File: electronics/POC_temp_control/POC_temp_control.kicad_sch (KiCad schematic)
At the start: 210 parts, among them J1 Conn_01x02, J2 Conn_01x07, J3 Conn_01x05, J4 Conn_01x06, J5 Conn_01x04, J6 Conn_01x06, Q1 PXT8050, Q10 BC847A, Q11 BC858B, Q12 BC847A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

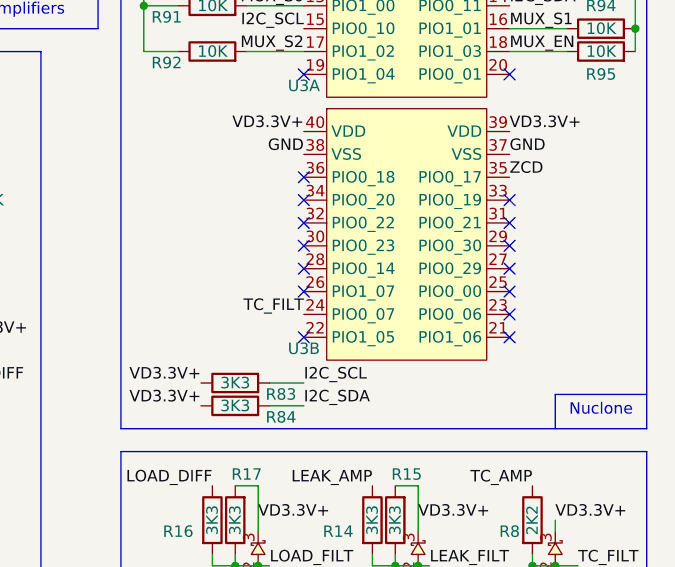
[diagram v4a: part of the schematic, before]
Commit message: further work on place and route, fixed some things with schematic
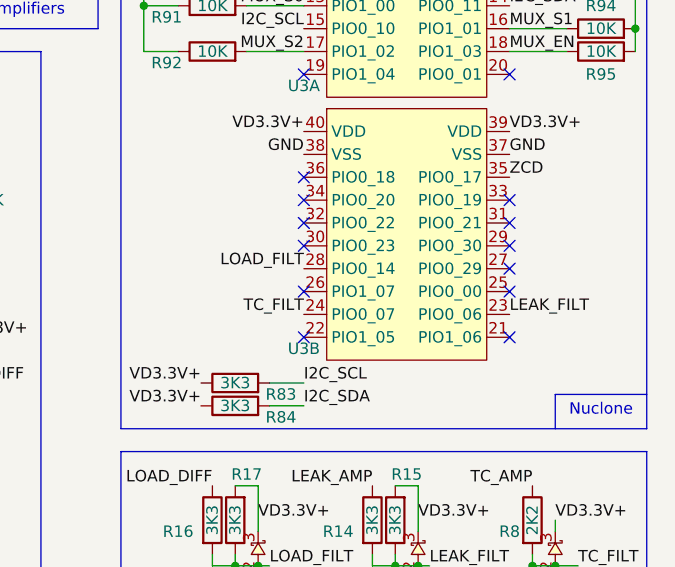
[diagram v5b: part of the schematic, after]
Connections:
- net LEAK_FILT: now also U3.23 (PIO0_06)
- net LOAD_FILT: now also U3.28 (PIO0_14)
- no-connect marks 33 -> 31
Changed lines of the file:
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@@
 	)
 	(no_connect
-		(at 245.11 62.23)
-	)
-	(no_connect
-		(at 267.97 67.31)
-	)
-	(no_connect
 		(at 245.11 69.85)
 	)
@@
 		)
 	)
+	(label "LEAK_FILT"
+		(at 267.97 67.31 0)
+		(fields_autoplaced yes)
+		(effects
+			(font
+				(size 1.27 1.27)
+			)
+			(justify left bottom)
+		)
+	)
 	(label "I2C_SCL"
 		(at 245.11 74.93 0)
@@
 		(fields_autoplaced yes)
 		(effects
+			(font
+				(size 1.27 1.27)
+			)
+			(justify right bottom)
+		)
+	)
+	(label "LOAD_FILT"
+		(at 245.11 62.23 180)
+		(fields_autoplaced yes)
+		(effects

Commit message: WIP further routing
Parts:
- removed R91, R92, R94, R95: 10K, SquantorResistor:R_0603_hand, symbol Device:R
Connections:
- net +5VD: no longer J2.2 (Pin_2)
- net VD5V+: now also J2.2 (Pin_2)

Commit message: WIP silk placement
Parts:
- D10: value GRN -> Power On
- H1, H2, H3, H4: value MountingHole -> M3
- TP7: value A7+ -> A7-
- TP8: value A5+ -> A5-
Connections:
- net +5VD is gone; now on net VD5V+: R9.2
- net SW_LOAD_1: now also U3.21 (PIO1_06)
- net SW_LOAD_2: now also U3.22 (PIO1_05)
- no-connect marks 31 -> 29
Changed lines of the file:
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@@
 	)
 	(no_connect
-		(at 245.11 69.85)
-	)
-	(no_connect
 		(at 92.71 110.49)
 	)
@@
 	)
 	(no_connect
-		(at 267.97 69.85)
-	)
-	(no_connect
 		(at 179.07 92.71)
 	)
@@
 		)
 	)
-	(label "+5VD"
+	(label "VD5V+"
 		(at 30.48 73.66 180)
 		(effects
@@
 		)
 	)
+	(label "SW_LOAD_1"
+		(at 267.97 69.85 0)
+		(effects
+			(font
+				(size 1.27 1.27)
+			)
+			(justify left bottom)
+		)
+	)
 	(label "LOAD1"
 		(at 92.71 92.71 0)
@@
 		)
 	)
+	(label "SW_LOAD_2"
+		(at 245.11 69.85 180)
+		(effects
+			(font
+				(size 1.27 1.27)
+			)
+			(justify right bottom)
+		)
+	)
 	(label "GND_SEN"
 		(at 163.83 97.79 180)
@@
 			)
 		)
-		(property "Value" "MountingHole"
+		(property "Value" "M3"
 			(at 139.7 180.34 0)
 			(effects
@@
 			)
 		)
-		(property "Value" "MountingHole"
+		(property "Value" "M3"
 			(at 139.7 175.2599 0)
 			(effects
@@
 			)
 		)
-		(property "Value" "MountingHole"
+		(property "Value" "M3"
 			(at 139.7 191.7699 0)
 			(effects
@@
 			)
 		)
-		(property "Value" "MountingHole"
+		(property "Value" "M3"
 			(at 146.05 186.69 90)
 			(effects
@@
 			)
 		)
-		(property "Value" "A5+"
+		(property "Value" "A5-"
 			(at 86.36 64.77 0)
 			(effects
@@
 			)
 		)
-		(property "Value" "GRN"
+		(property "Value" "Power On"
 			(at 246.38 127 90)
 			(effects
@@
 			)
 		)
-		(property "Value" "A7+"
+		(property "Value" "A7-"
 			(at 86.36 62.23 0)
 			(effects

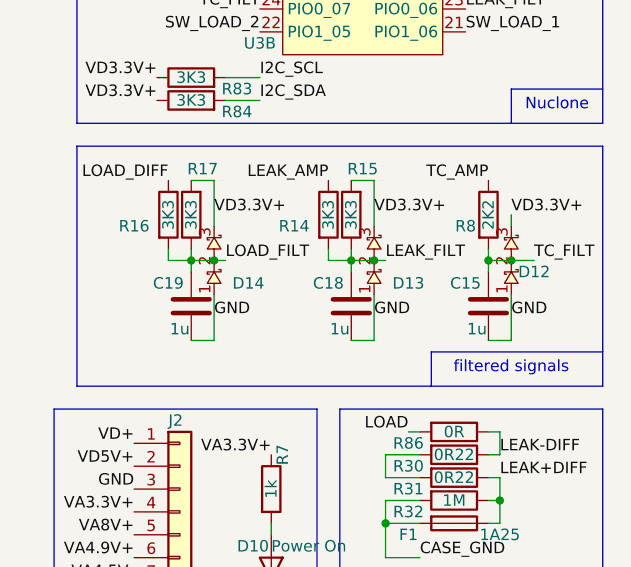
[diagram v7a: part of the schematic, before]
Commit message: updated silk placements and component values
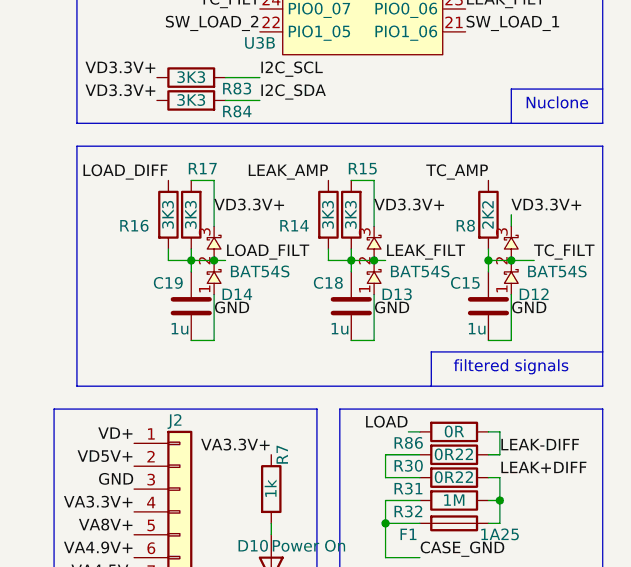
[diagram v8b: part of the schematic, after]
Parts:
- D12, D13, D14: value ~ -> BAT54S
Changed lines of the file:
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@@
 		(dnp no)
 		(property "Reference" "D13"
-			(at 261.62 97.79 0)
+			(at 260.35 99.06 0)
 			(effects
 				(font
@@
 			)
 		)
-		(property "Value" "~"
-			(at 260.35 96.393 0)
+		(property "Value" "BAT54S"
+			(at 262.89 96.52 0)
 			(effects
 				(font
 					(size 1.27 1.27)
 				)
-				(justify left)
 			)
 		)
@@
 		(dnp no)
 		(property "Reference" "D14"
-			(at 243.84 97.79 0)
+			(at 242.57 99.06 0)
 			(effects
 				(font
@@
 			)
 		)
-		(property "Value" "~"
-			(at 242.57 96.393 0)
+		(property "Value" "BAT54S"
+			(at 245.11 96.52 0)
 			(effects
 				(font
 					(size 1.27 1.27)
 				)
-				(justify left)
 			)
 		)
@@
 		(dnp no)
 		(property "Reference" "D12"
-			(at 275.59 96.52 0)
+			(at 275.59 99.06 0)
 			(effects
 				(font
@@
 			)
 		)
-		(property "Value" "~"
-			(at 275.59 96.393 0)
+		(property "Value" "BAT54S"
+			(at 278.13 96.52 0)
 			(effects
 				(font
 					(size 1.27 1.27)
 				)
-				(justify left)
 			)
 		)
